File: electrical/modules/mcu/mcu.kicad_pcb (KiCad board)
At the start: 2 copper layers, 23 parts, among them U201 STM32L452RCTx

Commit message: Redo layout of MCU module.
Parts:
- removed D201: Blue LED, LED_SMD:LED_0603_1608Metric
- removed R201: 33, footprints:Nondescript_R_0402_1005Metric
- added R202: 9k31, footprints:Nondescript_R_0402_1005Metric, F.Cu at (137.8, 96.2)
- added R203: 33, footprints:Nondescript_R_0402_1005Metric, F.Cu at (150.8, 85.7)
- added R204: 33, footprints:Nondescript_R_0402_1005Metric, F.Cu at (148.8, 85.7)
- added R207: 9k31, footprints:Nondescript_R_0402_1005Metric, F.Cu at (137.8, 98.2)
- added R213: 9k31, footprints:Nondescript_R_0402_1005Metric, F.Cu at (146.8, 83.9)
- added R217: 9k31, footprints:Nondescript_R_0402_1005Metric, F.Cu at (144.8, 83.9)
- moved C210 22.2 mm to (142.8, 88.4)
- moved C204 20.6 mm to (142.8, 89.4)
- moved C201 18.7 mm to (143.8, 86.4), turned to 180 degrees
- moved R212 17.2 mm to (147.5, 106.2)
- moved C208 15.5 mm to (151.3, 104.9), turned to 180 degrees
- moved C207 15.5 mm to (151.3, 103.9), turned to 180 degrees
- moved R214 15.0 mm to (149.5, 106.2), turned to 180 degrees
- moved C205 12.1 mm to (138.8, 98.9), turned to 90 degrees
- moved C202 11.2 mm to (139.8, 94.7), turned to 90 degrees
- moved C203 10.9 mm to (143.8, 104.9), turned to 180 degrees
- moved R208 10.7 mm to (156.1, 99.4)
- moved R205 10.2 mm to (138.8, 94.7), turned to -90 degrees
- moved R209 10.1 mm to (156.1, 100.4)
- moved R216 9.80 mm to (147.8, 85.7), turned to 90 degrees
- moved C209 9.48 mm to (139.8, 98.9), turned to 90 degrees
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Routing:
- net +3V3: track 0.00 -> 23.9 mm, vias 0 -> 16
- net GND: track 0.00 -> 21.7 mm, vias 0 -> 12
- net /BOOT0: track 0.00 -> 8.09 mm
- net /I2C1_SDA: track 0.00 -> 7.30 mm
- net /I2C1_SCL: track 0.00 -> 7.08 mm
- net /SWCLK: track 0.00 -> 6.70 mm
- net /PERIPH_INT_2: track 0.00 -> 6.70 mm
- net /SPI3_MISO: track 0.00 -> 6.28 mm
- net /CAN1_SILENT: track 0.00 -> 5.33 mm
- net /PERIPH_INT_1: track 0.00 -> 5.33 mm
- net /CAN1_TX: track 0.00 -> 5.33 mm
- net /CAN1_SHUTDOWN: track 0.00 -> 5.33 mm
- net /CAN1_RX: track 0.00 -> 5.33 mm
- net Net-(U201-PC10): track 0.00 -> 5.23 mm
- net Net-(U201-PC12): track 0.00 -> 4.81 mm
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
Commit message: Attempt to find a pattern to unify component designators. It looks like the best workflow will be to re-annotate the schematic of each module, sync the PCB to the schematic without relinking based on the designators, and then letting the board project use the designators directly, without re-annotating at that level. Need to investigate the effect of this workflow on the BOM and gerber files.
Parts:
- renumbered C201 to C101, C202 to C102, C203 to C103, C204 to C104, C205 to C105, C206 to C106, C207 to C107, C208 to C108, C209 to C109, C210 to C110, R202 to R101, R203 to R102, R204 to R103, R205 to R104, R206 to R105, R207 to R106, R209 to R107, R208 to R108, R210 to R109, R211 to R110, R212 to R111, R213 to R112, R214 to R113, R215 to R114, R216 to R115, R217 to R116, U201 to U101
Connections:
- net +3V3 renamed /3V3
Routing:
- net /3V3: vias 16 -> 0
- net (no net): vias 0 -> 16

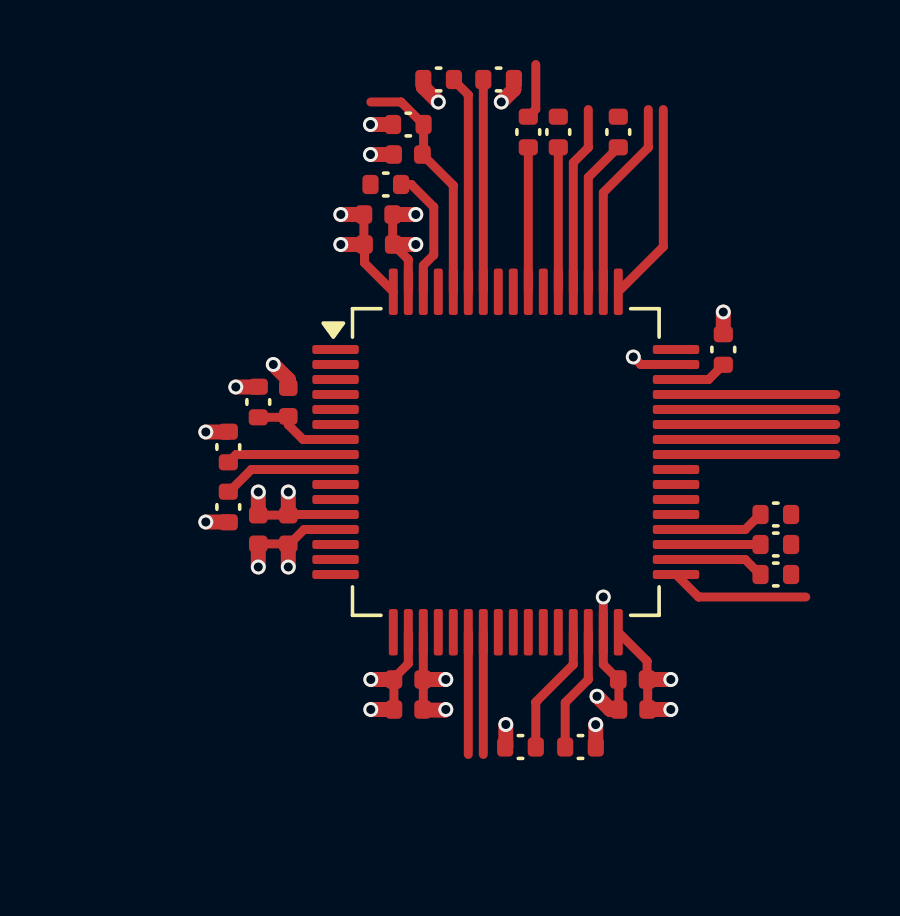
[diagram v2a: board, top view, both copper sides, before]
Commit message: Complete fanout of MCU and related passive components.
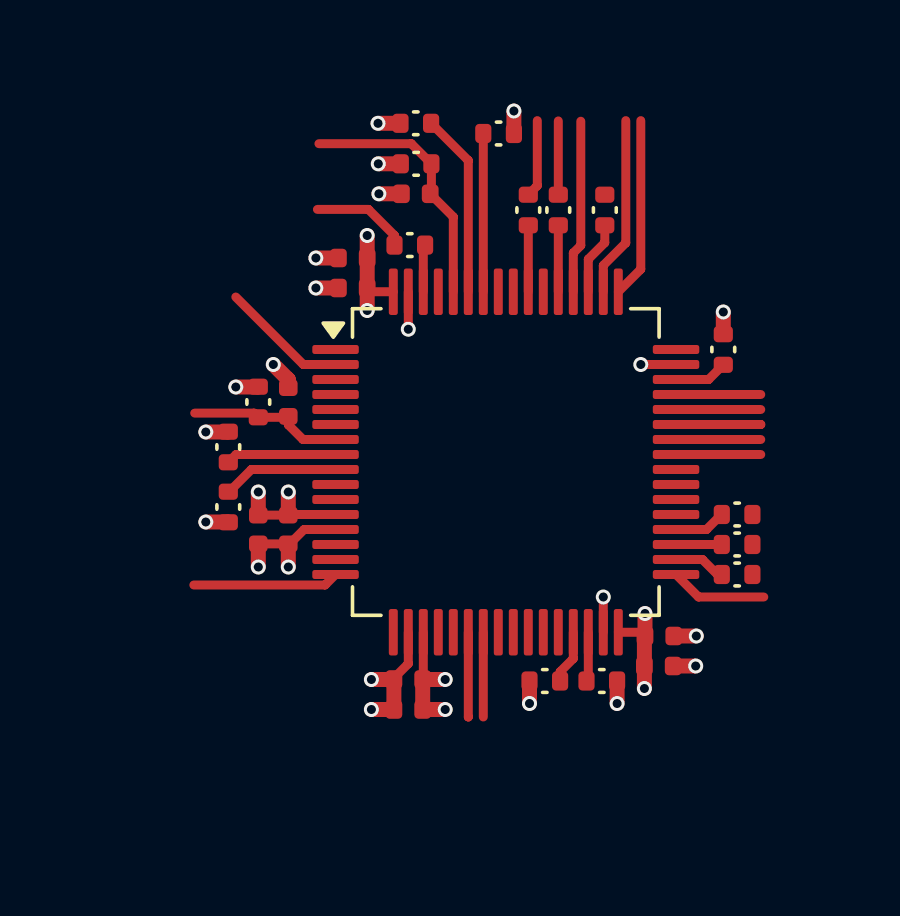
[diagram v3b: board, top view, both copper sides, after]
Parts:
- moved R102 2.64 mm to (150.3, 88.3)
- moved R103 2.60 mm to (148.8, 88.3)
- moved R115 2.60 mm to (147.8, 88.3)
- moved R111 2.34 mm to (148.3, 104.0)
- moved R113 2.31 mm to (150.2, 104.0)
- moved R110 2.17 mm to (143.8, 89.4)
- moved R112 1.80 mm to (146.8, 85.7)
- moved C107 1.70 mm to (152.2, 102.5), turned to 0 degrees
- moved C104 1.69 mm to (141.9, 90.9), turned to 180 degrees
- moved C110 1.68 mm to (141.9, 89.9), turned to 180 degrees
- moved C108 1.68 mm to (152.2, 103.5), turned to 0 degrees
- moved R116 1.65 mm to (144.1, 85.4)
- moved C101 1.34 mm to (144.1, 87.7)
- moved R105 1.34 mm to (144.1, 86.7)
- moved R107 1.29 mm to (154.8, 100.4)
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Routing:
- net /BOARD_ID_VERSION: track 0.00 -> 4.87 mm
- net /DEBUG_LED: track 0.00 -> 4.26 mm
- net GND: track 21.7 -> 17.5 mm, vias 12 -> 14
- net /BOOT0_CTRL: track 0.00 -> 3.25 mm
- net Net-(U101-PB9): track 4.37 -> 1.58 mm
- net Net-(U101-PC10): track 5.23 -> 2.44 mm
- net /3V3: track 23.9 -> 21.3 mm, vias 0 -> 16
- net Net-(U101-PC12): track 4.81 -> 2.22 mm
- net Net-(U101-PB3): track 4.81 -> 2.22 mm
- net /I2C2_SCL: track 4.34 -> 1.81 mm
- net /PERIPH_INT_1: track 5.33 -> 2.83 mm
- net /CAN1_TX: track 5.33 -> 2.83 mm
- net /CAN1_SHUTDOWN: track 5.33 -> 2.83 mm
- net /CAN1_RX: track 5.33 -> 2.83 mm
- net /CAN1_SILENT: track 5.33 -> 2.83 mm
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- added copper zone on In2.Cu, net /3V3
- added copper zone on In1.Cu, net GND
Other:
- copper layers 2 -> 4

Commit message: Restructure modules to get a reasonable core_board module.
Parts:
- removed R110: 33, footprints:Nondescript_R_0402_1005Metric
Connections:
- U101 pad 62: Net-(U101-PB9) -> unconnected-(U101-PB9-Pad62)
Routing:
- net /BOOT0: track 8.57 -> 4.54 mm
- net /BOOT0_CTRL: track 3.25 -> 0.00 mm
- net Net-(U101-PB9): track 1.58 -> 0.00 mm

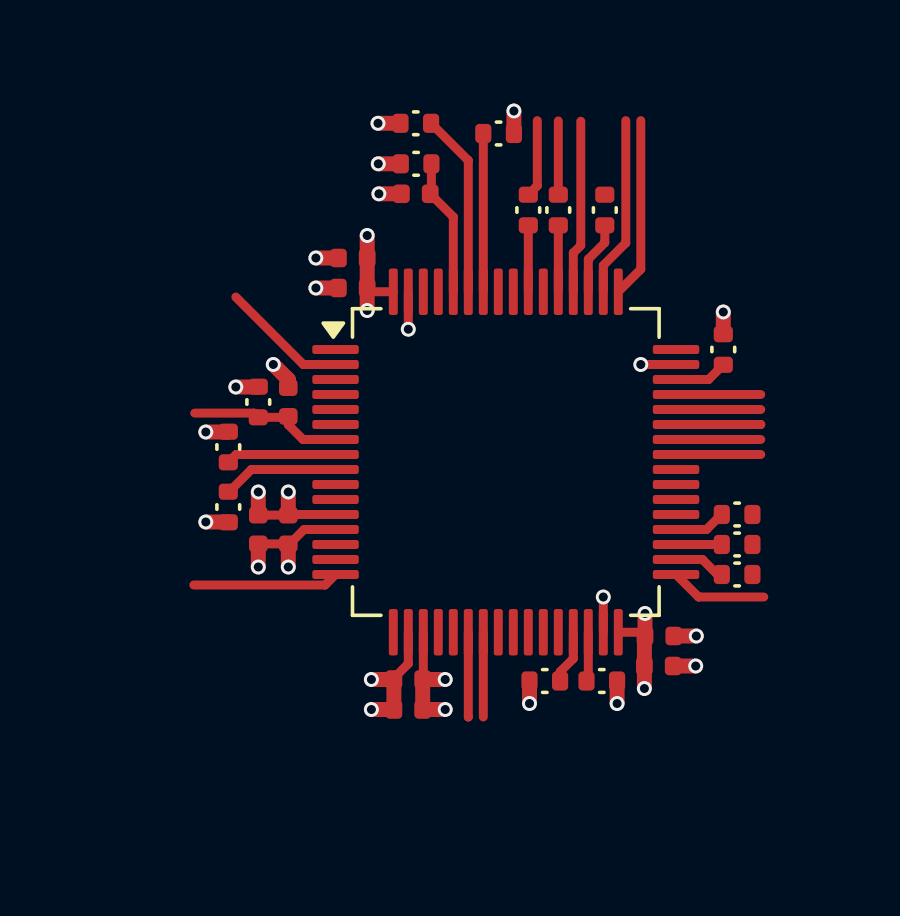
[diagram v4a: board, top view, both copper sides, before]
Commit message: Checkpoint work on 1s3p battery board. All components now have footprints and are laid out on the PCB. Many small errors still exist, and it is still missing auditing and review.
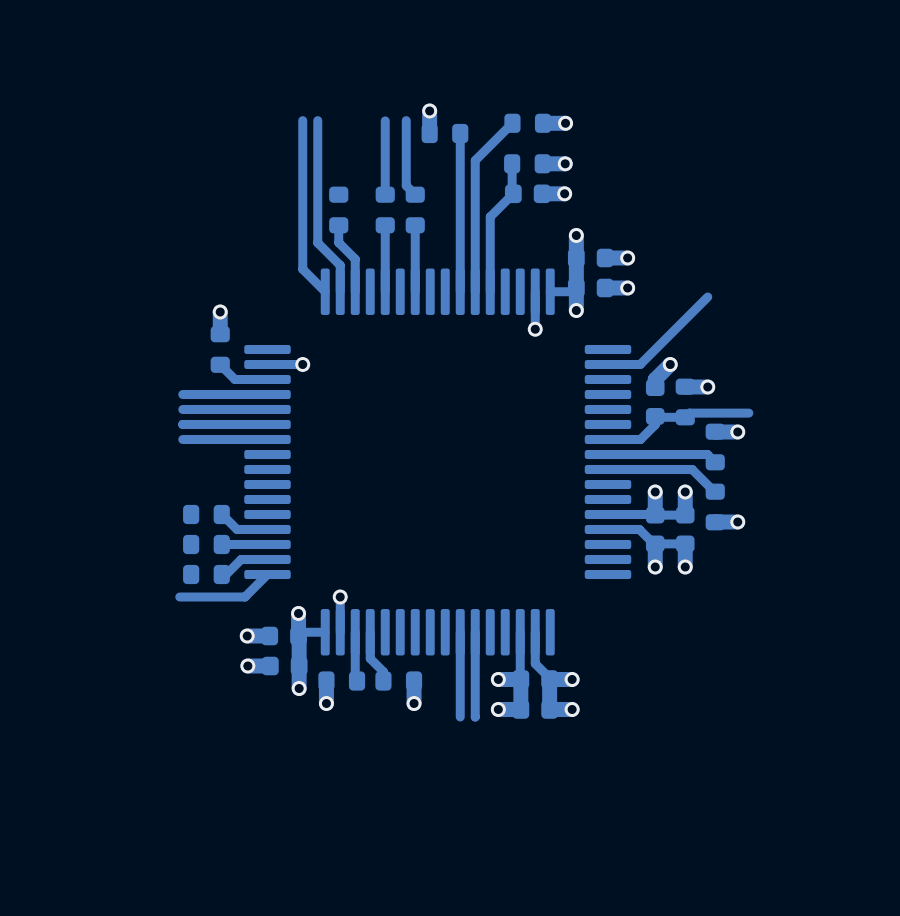
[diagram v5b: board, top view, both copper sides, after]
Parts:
- C101, C102, C103, C104, C105, C106, C107, C108, C109, C110, R101, R102, R103, R104, R105, R106, R107, R108, R109, R111, R112, R113, R114, R115, R116, U101: moved to B.Cu
- moved R107 17.7 mm to (137.1, 100.4), turned to 180 degrees
- moved R108 17.7 mm to (137.1, 99.4), turned to 180 degrees
- moved R109 17.7 mm to (137.1, 98.4), turned to 180 degrees
- moved R114 16.8 mm to (137.5, 92.9)
- moved R101 16.2 mm to (154.0, 96.2)
- moved R106 16.2 mm to (154.0, 98.2)
- moved C105 14.2 mm to (153.0, 98.9)
- moved R104 14.2 mm to (153.0, 94.7)
- moved C107 12.5 mm to (139.7, 102.5), turned to 180 degrees
- moved C108 12.5 mm to (139.7, 103.5), turned to 180 degrees
- moved C102 12.2 mm to (152.0, 94.7)
- moved C109 12.2 mm to (152.0, 98.9)
- moved R102 8.87 mm to (141.5, 88.3)
- moved R113 8.67 mm to (141.6, 104.0), turned to 0 degrees
- moved C104 7.93 mm to (149.9, 90.9), turned to 0 degrees
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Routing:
- net /SPI3_MISO: track 5.79 -> 0.00 mm
- net /BOARD_ID_VERSION: track 4.87 -> 0.00 mm
- net /PERIPH_INT_1: track 2.83 -> 0.00 mm

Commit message: Start sequence to synchronize UUIDs in modules so that ProjectInstances doesn't fail to import PCB layout.
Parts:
- renumbered C101 to C501, C102 to C502, C103 to C503, C104 to C504, C105 to C505, C106 to C506, C107 to C507, C108 to C508, C109 to C509, C110 to C510, R101 to R501, R102 to R502, R103 to R503, R104 to R504, R105 to R505, R106 to R506, R107 to R507, R108 to R508, R109 to R509, R111 to R510, R112 to R511, R113 to R512, R114 to R513, R115 to R514, R116 to R515, U101 to U501
